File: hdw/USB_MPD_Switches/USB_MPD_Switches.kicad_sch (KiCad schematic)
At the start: 0 parts

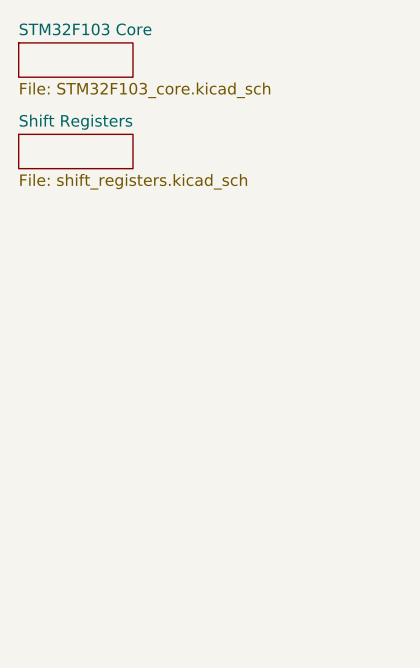
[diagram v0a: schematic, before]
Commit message: added cap touch stuff
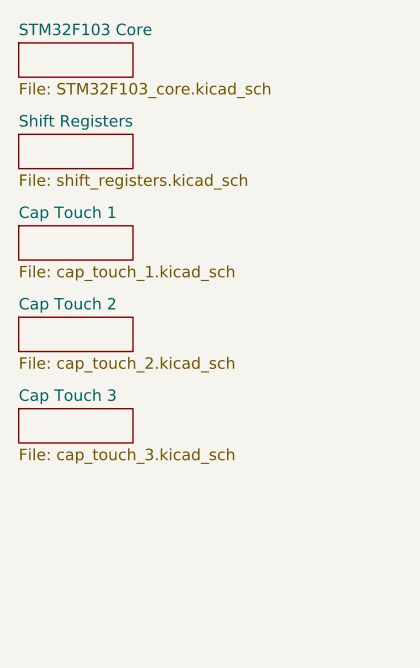
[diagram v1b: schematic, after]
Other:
- added sheet Cap Touch 1 (cap_touch_1.kicad_sch)
- added sheet Cap Touch 2 (cap_touch_2.kicad_sch)
- added sheet Cap Touch 3 (cap_touch_3.kicad_sch)
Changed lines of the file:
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@@
     (company "Drew Maatman")
+  )
+  (sheet (at 34.925 68.58) (size 12.7 3.81) (fields_autoplaced)
+    (stroke (width 0.1524) (type solid))
+    (fill (color 0 0 0 0.0000))
+    (property "Sheetname" "Cap Touch 3" (at 34.925 67.8684 0)
+      (effects (font (size 1.27 1.27)) (justify left bottom))
+    )
+    (property "Sheetfile" "cap_touch_3.kicad_sch" (at 34.925 72.9746 0)
+      (effects (font (size 1.27 1.27)) (justify left top))
+    )
+    (instances
+      (project "USB_MPD_Switches"
+        (path "/62d9a549-2742-4d98-96b6-bf7a87f3799a" (page "6"))
+      )
+    )
+  )
+  (sheet (at 34.925 48.26) (size 12.7 3.81) (fields_autoplaced)
+    (stroke (width 0.1524) (type solid))
+    (fill (color 0 0 0 0.0000))
+    (property "Sheetname" "Cap Touch 1" (at 34.925 47.5484 0)
+      (effects (font (size 1.27 1.27)) (justify left bottom))
+    )
+    (property "Sheetfile" "cap_touch_1.kicad_sch" (at 34.925 52.6546 0)
+      (effects (font (size 1.27 1.27)) (justify left top))
+    )
+    (instances
+      (project "USB_MPD_Switches"
+        (path "/62d9a549-2742-4d98-96b6-bf7a87f3799a" (page "4"))
+      )
+    )
+  )
+  (sheet (at 34.925 58.42) (size 12.7 3.81) (fields_autoplaced)
+    (stroke (width 0.1524) (type solid))
+    (fill (color 0 0 0 0.0000))
+    (property "Sheetname" "Cap Touch 2" (at 34.925 57.7084 0)
+      (effects (font (size 1.27 1.27)) (justify left bottom))
+    )
+    (property "Sheetfile" "cap_touch_2.kicad_sch" (at 34.925 62.8146 0)
+      (effects (font (size 1.27 1.27)) (justify left top))
+    )
+    (instances
+      (project "USB_MPD_Switches"
+        (path "/62d9a549-2742-4d98-96b6-bf7a87f3799a" (page "5"))
+      )
+    )
   )
   (sheet (at 34.925 27.94) (size 12.7 3.81) (fields_autoplaced)

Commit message: added USB port, +3.3V power supply
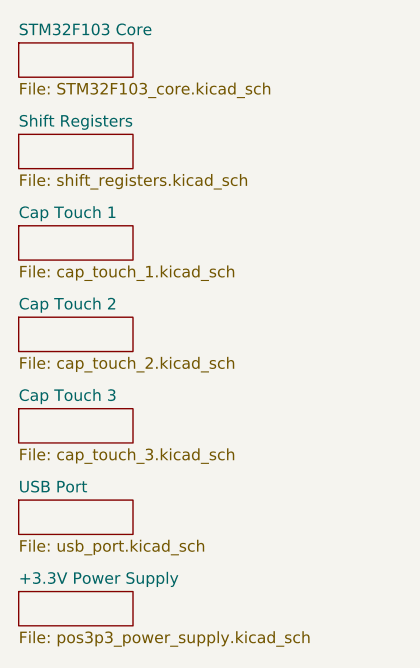
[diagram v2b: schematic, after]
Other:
- added sheet +3.3V Power Supply (pos3p3_power_supply.kicad_sch)
- added sheet USB Port (usb_port.kicad_sch)
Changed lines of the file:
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@@
   (title_block
     (title "USB MPD")
-    (date "2024-02-01")
+    (date "2024-02-06")
     (rev "PRELIM")
     (company "Drew Maatman")
@@
     )
   )
+  (sheet (at 34.925 88.9) (size 12.7 3.81) (fields_autoplaced)
+    (stroke (width 0.1524) (type solid))
+    (fill (color 0 0 0 0.0000))
+    (property "Sheetname" "+3.3V Power Supply" (at 34.925 88.1884 0)
+      (effects (font (size 1.27 1.27)) (justify left bottom))
+    )
+    (property "Sheetfile" "pos3p3_power_supply.kicad_sch" (at 34.925 93.2946 0)
+      (effects (font (size 1.27 1.27)) (justify left top))
+    )
+    (instances
+      (project "USB_MPD_Switches"
+        (path "/62d9a549-2742-4d98-96b6-bf7a87f3799a" (page "8"))
+      )
+    )
+  )
   (sheet (at 34.925 38.1) (size 12.7 3.81) (fields_autoplaced)
     (stroke (width 0.1524) (type solid))
@@
       )
     )
+  )
+  (sheet (at 34.925 78.74) (size 12.7 3.81) (fields_autoplaced)
+    (stroke (width 0.1524) (type solid))
+    (fill (color 0 0 0 0.0000))
+    (property "Sheetname" "USB Port" (at 34.925 78.0284 0)
+      (effects (font (size 1.27 1.27)) (justify left bottom))
+    )
+    (property "Sheetfile" "usb_port.kicad_sch" (at 34.925 83.1346 0)
+      (effects (font (size 1.27 1.27)) (justify left top))
+    )
+    (instances
+      (project "USB_MPD_Switches"
+        (path "/62d9a549-2742-4d98-96b6-bf7a87f3799a" (page "7"))
+      )
+    )
